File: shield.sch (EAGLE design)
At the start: 14 parts, among them X1 22-03-5035, X2 22-03-5035, Y1 22-03-5035, Y2 22-03-5035

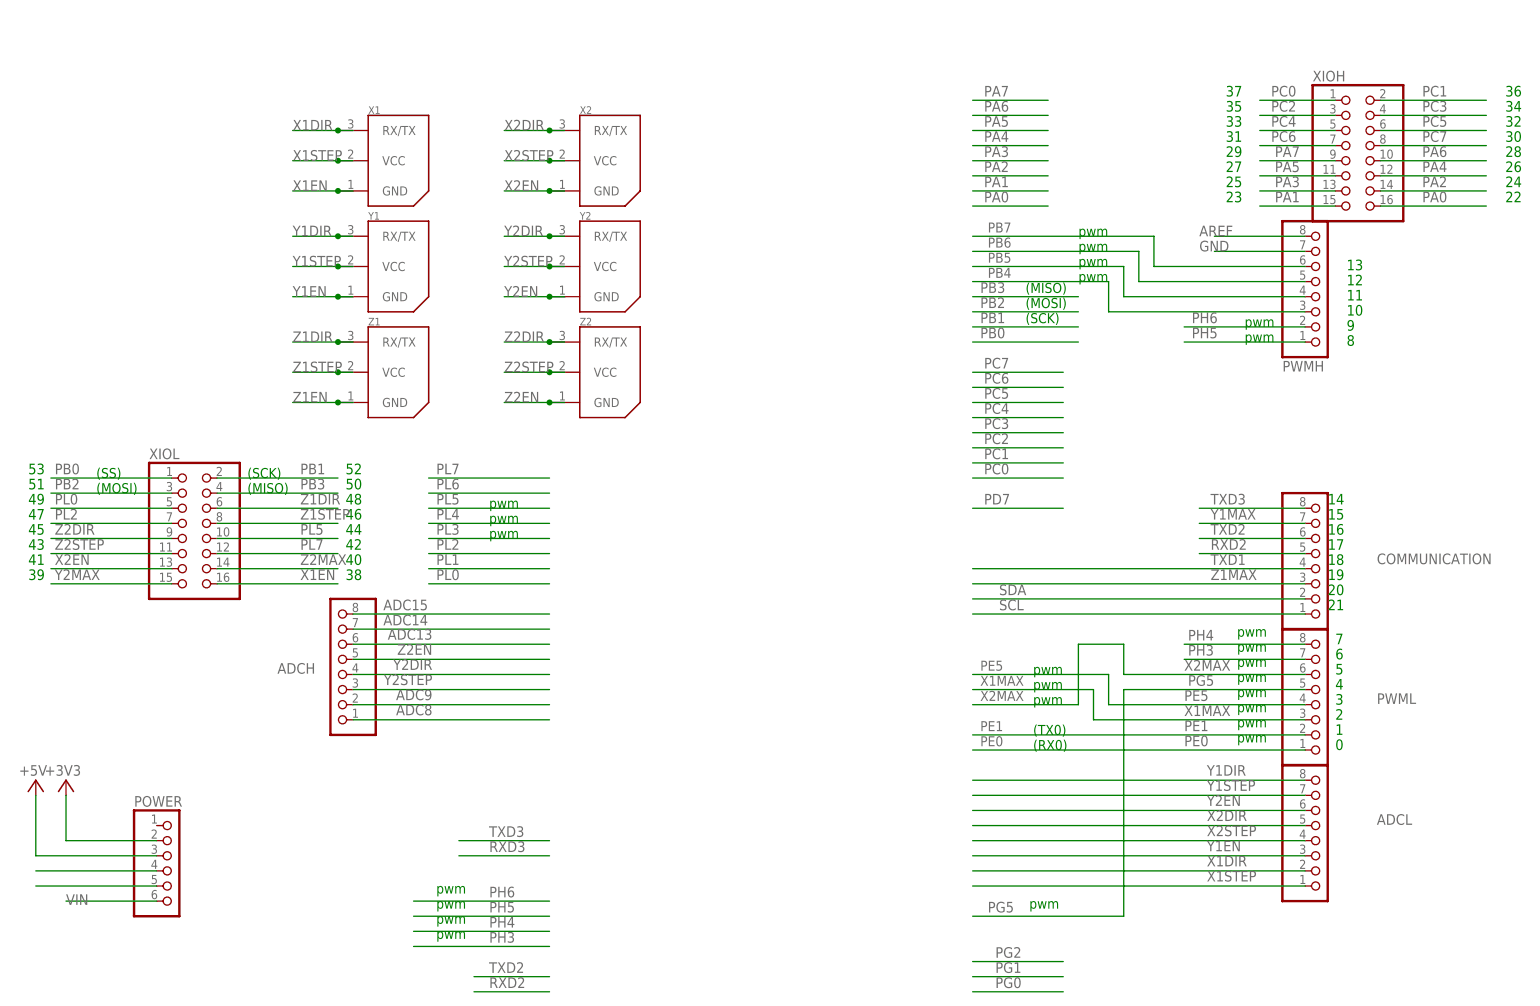
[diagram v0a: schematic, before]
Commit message: change to 4 pin header
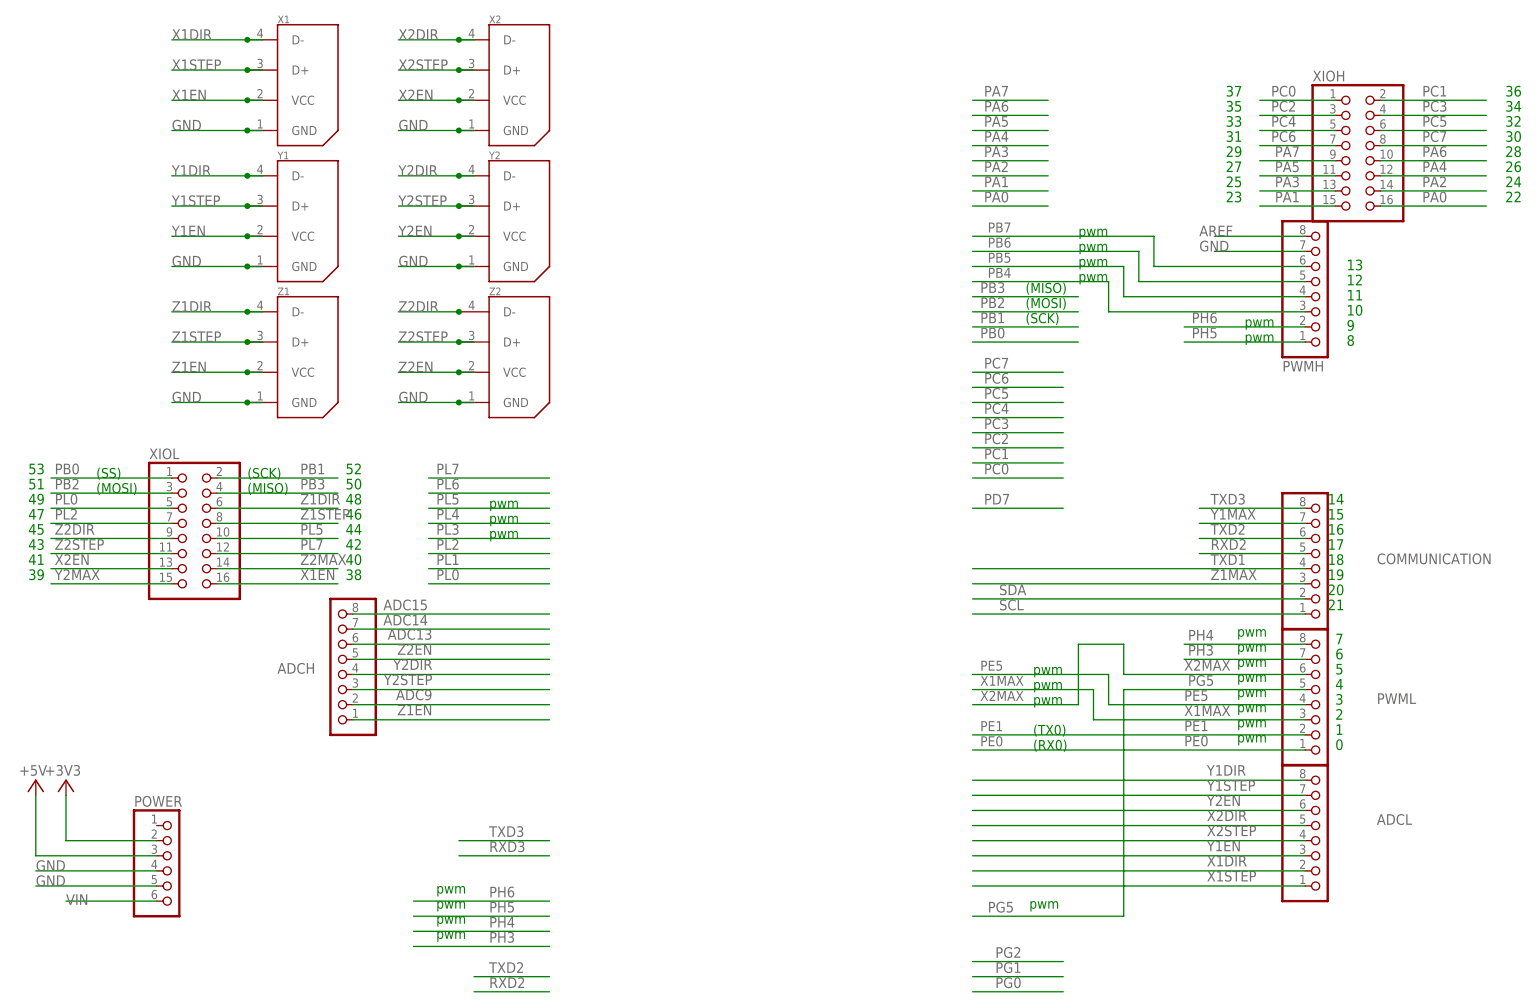
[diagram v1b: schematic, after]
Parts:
- X1, X2, Y1, Y2, Z1, Z2: value 22-03-5035 -> 22-03-5045; device molex:22-03-5035 -> molex:22-03-5045
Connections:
- removed net ADC8: ADCH.1
- removed net N$1: POWER.5
- removed net N$2: POWER.4
- net GND: now also POWER.4, POWER.5, X1.GND, X2.GND, Y1.GND, Y2.GND, Z1.GND, Z2.GND
- net X1DIR: now also X1.D-; no longer X1.RX/TX
- net X1EN: now also X1.VCC; no longer X1.GND
- net X1STEP: now also X1.D+; no longer X1.VCC
- net X2DIR: now also X2.D-; no longer X2.RX/TX
- net X2EN: now also X2.VCC; no longer X2.GND
- net X2STEP: now also X2.D+; no longer X2.VCC
- net Y1DIR: now also Y1.D-; no longer Y1.RX/TX
- net Y1EN: now also Y1.VCC; no longer Y1.GND
- net Y1STEP: now also Y1.D+; no longer Y1.VCC
- net Y2DIR: now also Y2.D-; no longer Y2.RX/TX
- net Y2EN: now also Y2.VCC; no longer Y2.GND
- net Y2STEP: now also Y2.D+; no longer Y2.VCC
- net Z1DIR: now also Z1.D-; no longer Z1.RX/TX
- net Z1EN: now also ADCH.1, Z1.VCC; no longer Z1.GND
- net Z1STEP: now also Z1.D+; no longer Z1.VCC
- net Z2DIR: now also Z2.D-; no longer Z2.RX/TX
- net Z2EN: now also Z2.VCC; no longer Z2.GND
- net Z2STEP: now also Z2.D+; no longer Z2.VCC
